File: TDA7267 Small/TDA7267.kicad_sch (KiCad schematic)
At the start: 18 parts, among them U1 TDA7267

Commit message: More stuff
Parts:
- D1: footprint LED_THT:LED_D5.0mm -> LED_THT:LED_D3.0mm
- RV1: value A10K -> R_Potentiometer
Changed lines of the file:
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@@
 			)
 		)
-		(property "Value" "A10K"
+		(property "Value" "R_Potentiometer"
 			(at 73.66 87.6299 0)
 			(effects
@@
 			)
 		)
-		(property "Footprint" "LED_THT:LED_D5.0mm"
+		(property "Footprint" "LED_THT:LED_D3.0mm"
 			(at 138.43 63.5 0)
 			(effects

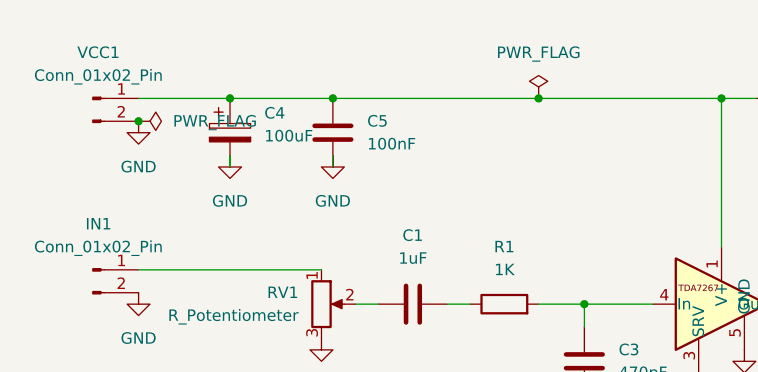
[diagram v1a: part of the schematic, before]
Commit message: Bottom GND plane
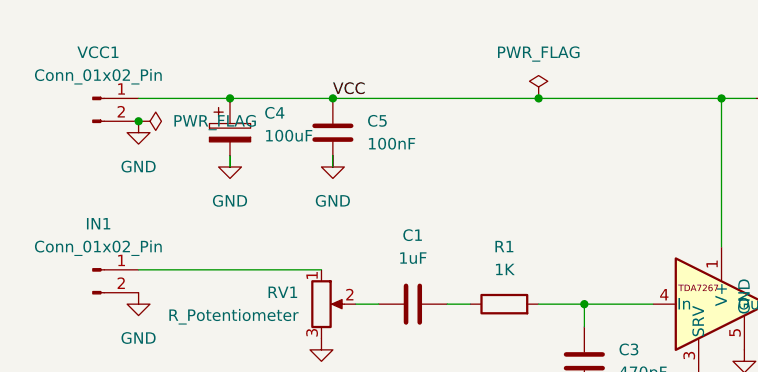
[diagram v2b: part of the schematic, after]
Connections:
- net VCC: now reaches C4.1, C5.2, R2.2, U1.1 (V+), VCC1.1 (Pin_1)
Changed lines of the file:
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@@
+		)
+	)
+	(label "VCC"
+		(at 77.47 63.5 0)
+		(effects
+			(font
+				(size 1.27 1.27)
+			)
+			(justify left bottom)
 		)
 	)
